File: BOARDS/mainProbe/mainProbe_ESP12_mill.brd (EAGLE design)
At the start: 37.8 x 55.9 mm, 18 parts

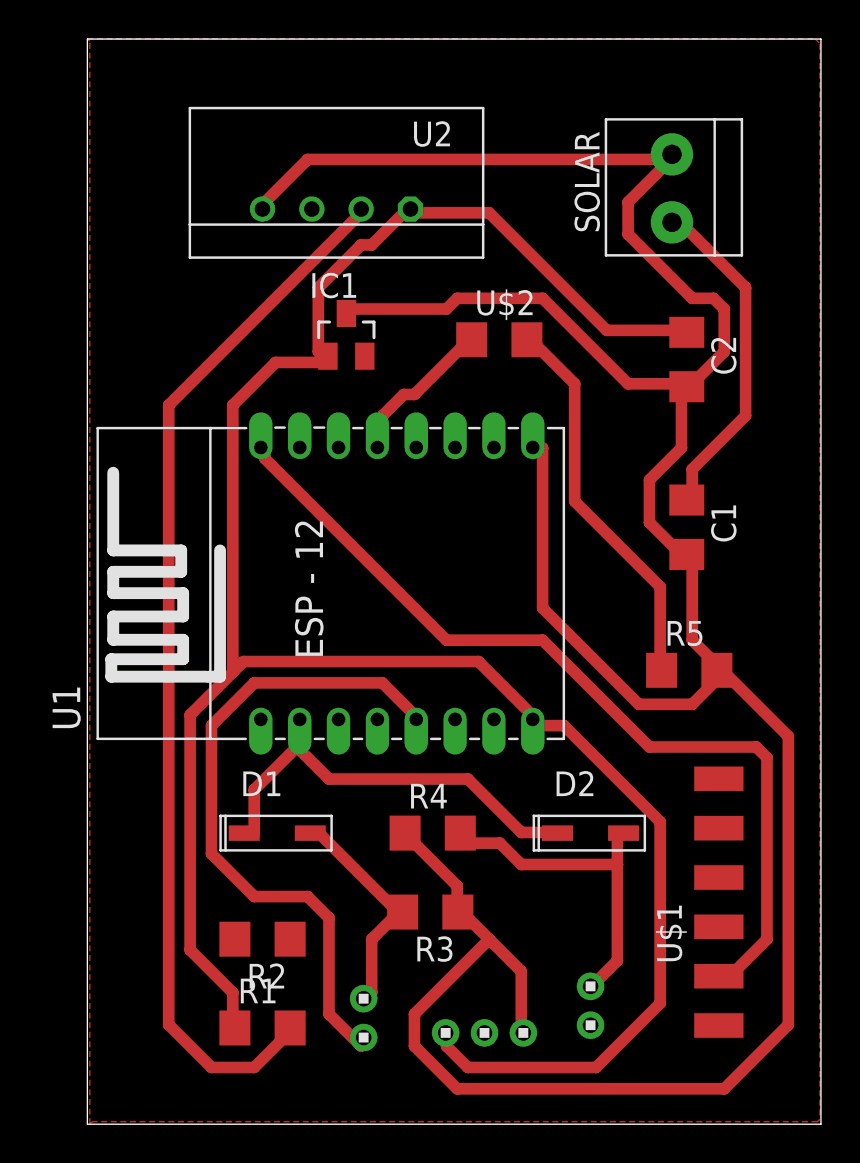
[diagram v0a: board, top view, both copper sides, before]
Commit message: placa com headers thanks to FS
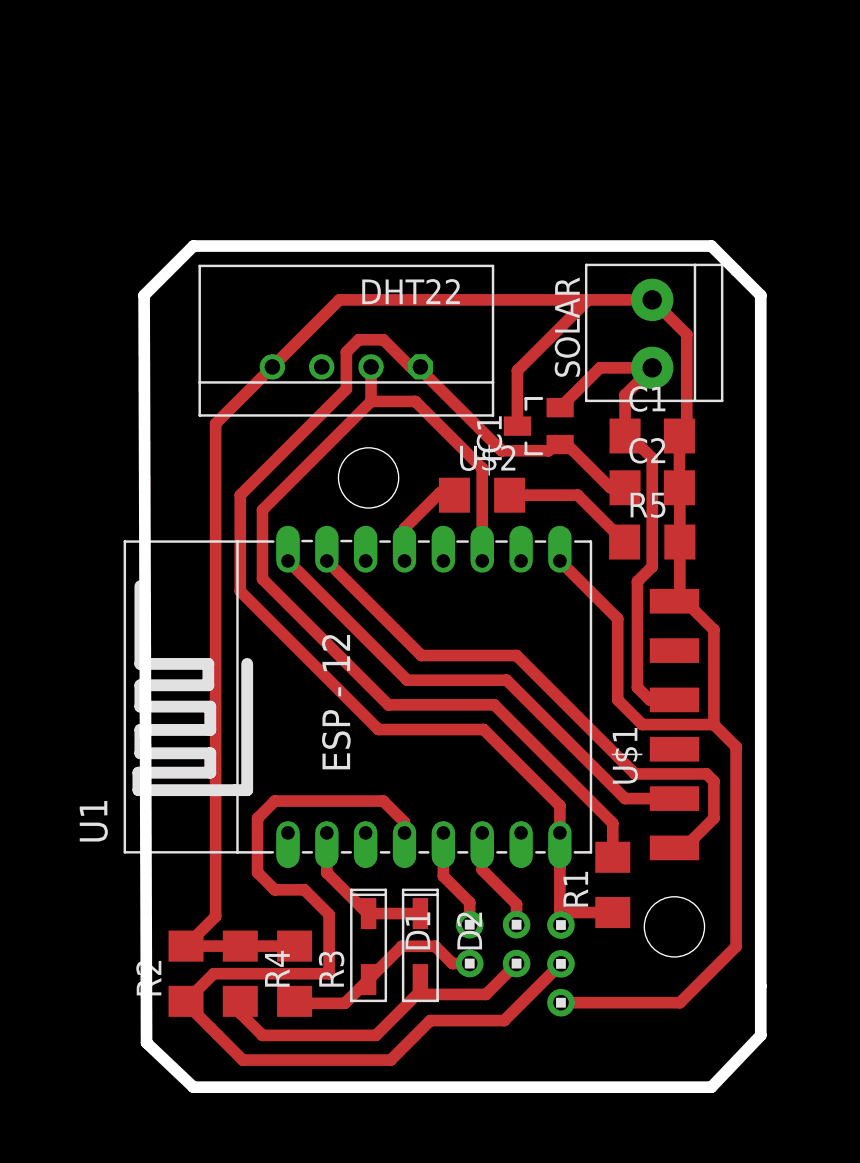
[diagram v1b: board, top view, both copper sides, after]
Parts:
- removed U2: (no value), RHT03_DHT-22_AM2302:RHT03_DHT-22
- added DHT22: (no value), RHT03_DHT-22_AM2302:RHT03_DHT-22
- moved R1 19.5 mm to (24.5, 11.0), turned to 90 degrees
- moved R4 12.3 mm to (5.33, 6.48), turned to 270 degrees
- moved IC1 11.0 mm to (20.7, 34.7), turned to 90 degrees
- moved D2 10.5 mm to (14.6, 7.87), turned to 270 degrees
- moved U$1 9.43 mm to (27.7, 19.3)
- moved U$2 8.05 mm to (17.8, 31.1)
- moved R3 7.67 mm to (8.13, 6.48), turned to 270 degrees
- moved SOLAR 7.56 mm to (26.5, 39.4)
- moved D1 7.50 mm to (11.9, 7.87), turned to 270 degrees
- moved R5 6.87 mm to (26.5, 28.7)
- moved C2 6.84 mm to (26.5, 31.5), turned to 0 degrees
- moved MOISTURE1 6.66 mm to (17.1, 8.00), turned to 270 degrees
- moved U1 6.01 mm to (13.6, 20.8)
- moved TEMPSENSOR 5.31 mm to (21.8, 6.99), turned to 270 degrees
- moved C1 5.02 mm to (26.5, 34.2), turned to 0 degrees
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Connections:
- net 3.3V: now also DHT22.VDD; no longer U2.VDD
- net GND: now also DHT22.GND; no longer U2.GND
- net N$8: now also DHT22.DATA; no longer U2.DATA
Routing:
- net 3.3V: track 115.4 -> 61.9 mm
- net N$3: track 0.00 -> 50.3 mm
- net GND: track 157.6 -> 126.4 mm
- net RX: track 0.00 -> 29.2 mm
- net ONMOIST1: track 34.1 -> 5.29 mm
- net TX: track 45.9 -> 25.0 mm
- net ADC: track 23.9 -> 7.74 mm
- net N$6: track 20.0 -> 6.92 mm
- net VIN: track 17.3 -> 25.8 mm
- net ONMOIST2: track 0.00 -> 5.46 mm
- net N$8: track 54.2 -> 50.2 mm
- net LED1: track 7.89 -> 5.06 mm
- net N$5: track 11.8 -> 10.6 mm
- net N$7: track 17.6 -> 18.3 mm
- removed copper zone on layer 1, net GND
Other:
- board size 37.8 x 55.9 mm -> 31.8 x 43.3 mm
